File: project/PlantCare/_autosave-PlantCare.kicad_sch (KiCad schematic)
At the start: 34 parts, among them J1 Conn_01x06_Female, J2 USB_C_6pin, J3 Conn_01x02_Female, SW1 SW_DPDT_x2, SW2 SW_Push, SW3 SW_Push, U1 SPX3819M5-L-3-3, U2 ESP-12E, U3 TFT_1.3_12, U4 TP4056_[C16581]

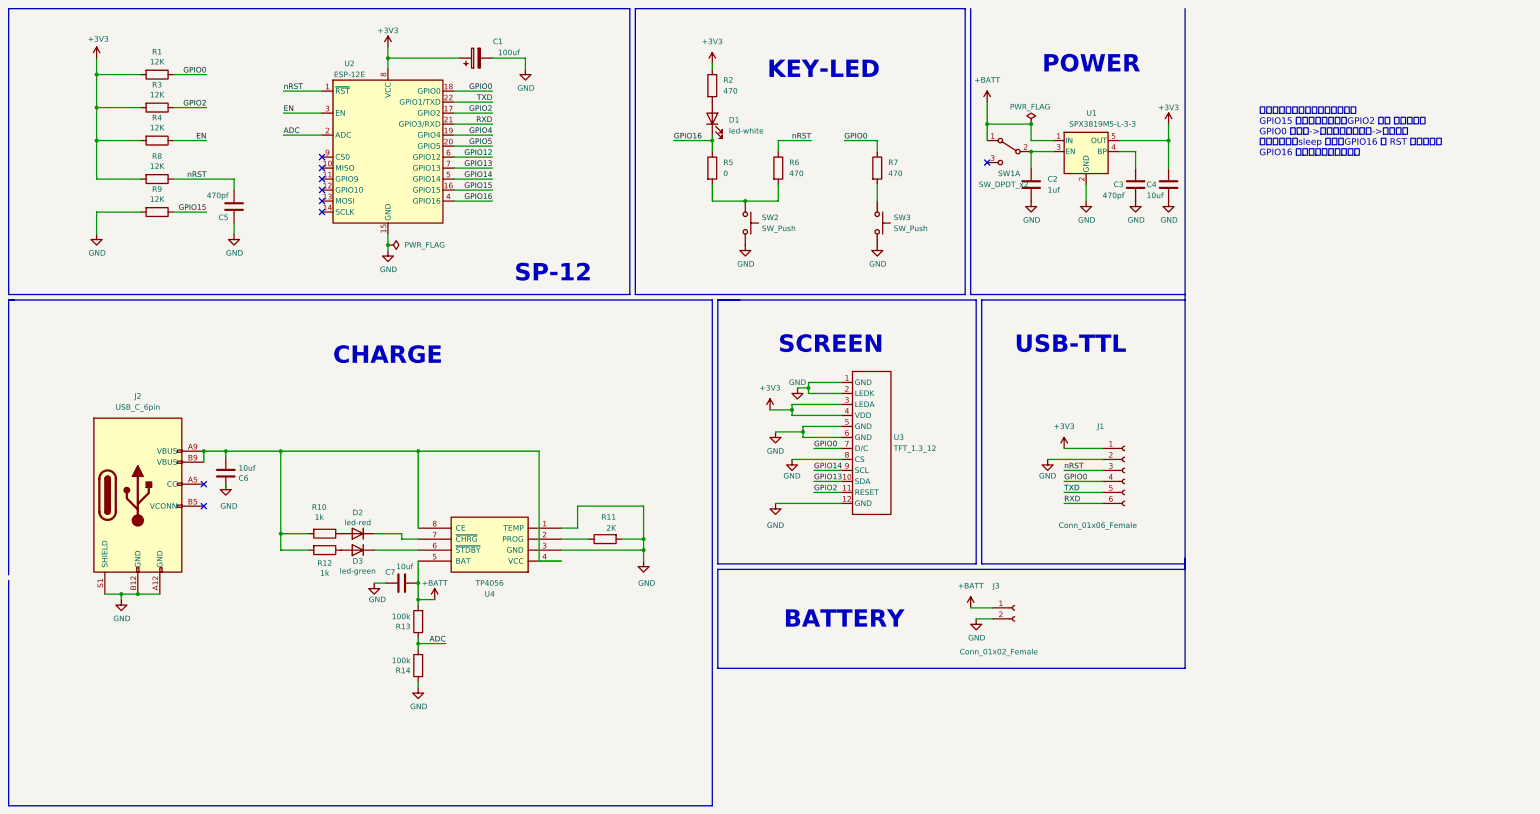
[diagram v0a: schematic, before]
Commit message: fix: screen rst and cs
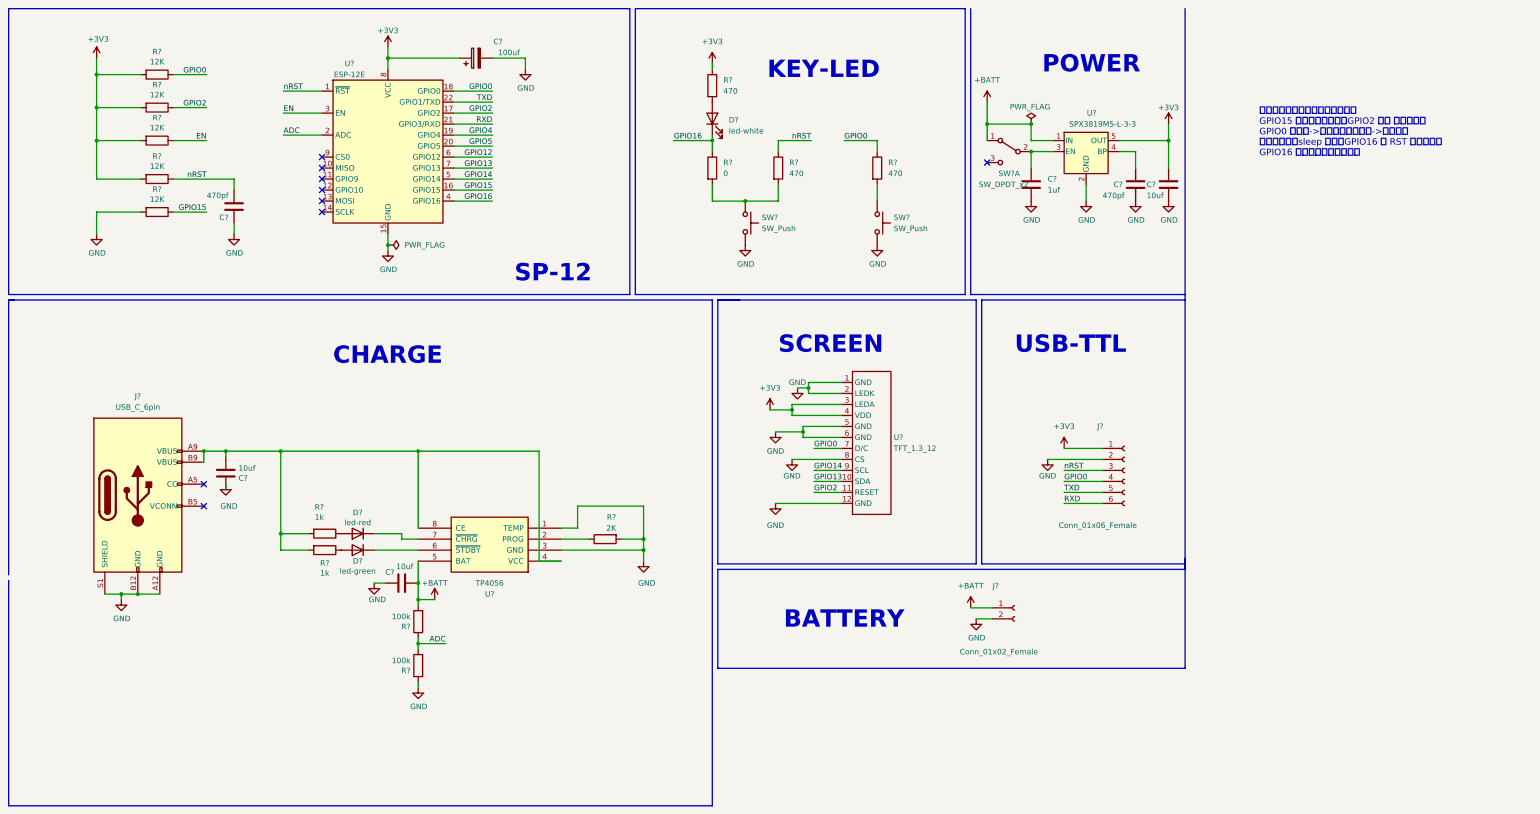
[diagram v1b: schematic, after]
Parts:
- removed C1: 100uf, lc_lib:CASE-B_3528, symbol Device:C_Polarized
- removed C2: 1uf, Capacitor_SMD:C_0402_1005Metric, symbol Device:C
- removed C3, C5: 470pf, Capacitor_SMD:C_0402_1005Metric, symbol Device:C
- removed C4, C6, C7: 10uf, Capacitor_SMD:C_0402_1005Metric, symbol Device:C
- removed D1: led-white, LED_SMD:LED_0402_1005Metric, symbol Device:LED
- removed D2: led-red, LED_SMD:LED_0402_1005Metric, symbol Device:D
- removed D3: led-green, LED_SMD:LED_0402_1005Metric, symbol Device:D
- removed J1: Conn_01x06_Female, Connector_PinHeader_1.27mm:PinHeader_1x06_P1.27mm_Vertical, symbol Connector:Conn_01x06_Female
- removed J2: USB_C_6pin, My-lib-footprints:USB_C_6pin, symbol My-lib:USB_C_6pin
- removed J3: Conn_01x02_Female, Connector_PinHeader_2.54mm:PinHeader_1x02_P2.54mm_Vertical, symbol Connector:Conn_01x02_Female
- removed R1, R3, R4, R8, R9: 12K, Resistor_SMD:R_0402_1005Metric, symbol Device:R
- removed R10, R12: 1k, Resistor_SMD:R_0402_1005Metric, symbol Device:R
- removed R11: 2K, Resistor_SMD:R_0402_1005Metric, symbol Device:R
- removed R13, R14: 100k, Resistor_SMD:R_0402_1005Metric, symbol Device:R
- removed R2, R6, R7: 470, Resistor_SMD:R_0402_1005Metric, symbol Device:R
- removed R5: 0, Resistor_SMD:R_0402_1005Metric, symbol Device:R
- removed SW1: SW_DPDT_x2, Button_Switch_SMD:SW_SPDT_PCM12, symbol Switch:SW_DPDT_x2
- removed SW2, SW3: SW_Push, My-lib:Button_SMD,3x4x2mm, symbol Switch:SW_Push
- removed U1: SPX3819M5-L-3-3, Package_TO_SOT_SMD:SOT-23-5, symbol Regulator_Linear:SPX3819M5-L-3-3
- removed U2: ESP-12E, RF_Module:ESP-12E, symbol RF_Module:ESP-12E
- removed U3: TFT_1.3_12, My-lib-footprints:TFT_1.3_12_front, symbol My-lib:TFT_1.3_12
- removed U4: TP4056_[C16581], lc_lib:SOP-8_EP_150MIL, symbol lc_IC:TP4056_[C16581]
- added C?: 100uf, lc_lib:CASE-B_3528, symbol Device:C_Polarized
- added C? (x3): 10uf, Capacitor_SMD:C_0402_1005Metric, symbol Device:C
- added C? (x2): 470pf, Capacitor_SMD:C_0402_1005Metric, symbol Device:C
- added C?: 1uf, Capacitor_SMD:C_0402_1005Metric, symbol Device:C
- added D?: led-red, LED_SMD:LED_0402_1005Metric, symbol Device:D
- added D?: led-white, LED_SMD:LED_0402_1005Metric, symbol Device:LED
- added D?: led-green, LED_SMD:LED_0402_1005Metric, symbol Device:D
- added J?: Conn_01x02_Female, Connector_PinHeader_2.54mm:PinHeader_1x02_P2.54mm_Vertical, symbol Connector:Conn_01x02_Female
- added J?: USB_C_6pin, My-lib-footprints:USB_C_6pin, symbol My-lib:USB_C_6pin
- added J?: Conn_01x06_Female, Connector_PinHeader_1.27mm:PinHeader_1x06_P1.27mm_Vertical, symbol Connector:Conn_01x06_Female
- added R? (x3): 470, Resistor_SMD:R_0402_1005Metric, symbol Device:R
- added R? (x5): 12K, Resistor_SMD:R_0402_1005Metric, symbol Device:R
- added R?: 2K, Resistor_SMD:R_0402_1005Metric, symbol Device:R
- added R? (x2): 1k, Resistor_SMD:R_0402_1005Metric, symbol Device:R
- added R?: 0, Resistor_SMD:R_0402_1005Metric, symbol Device:R
- added R? (x2): 100k, Resistor_SMD:R_0402_1005Metric, symbol Device:R
- added SW? (x2): SW_Push, My-lib:Button_SMD,3x4x2mm, symbol Switch:SW_Push
- added SW?: SW_DPDT_x2, Button_Switch_SMD:SW_SPDT_PCM12, symbol Switch:SW_DPDT_x2
- added U?: ESP-12E, RF_Module:ESP-12E, symbol RF_Module:ESP-12E
- added U?: TFT_1.3_12, My-lib-footprints:TFT_1.3_12_front, symbol My-lib:TFT_1.3_12
- added U?: TP4056_[C16581], lc_lib:SOP-8_EP_150MIL, symbol lc_IC:TP4056_[C16581]
- added U?: SPX3819M5-L-3-3, Package_TO_SOT_SMD:SOT-23-5, symbol Regulator_Linear:SPX3819M5-L-3-3
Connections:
- net +3V3: now also C?.1, C?.1, J?.1 (Pin_1), R?.1, R?.2, R?.2, R?.2, R?.2, U?.3 (LEDA), U?.4 (VDD), U?.5 (OUT), U?.8 (VCC)
- net +BATT: now also C?.1, J?.1 (Pin_1), R?.2, SW?.1 (A), U?.1 (IN), U?.5 (BAT)
- net ADC: now also R?.1, R?.2, U?.2 (ADC)
- net EN: now also R?.1, U?.3 (EN)
- net GND: now also C?.1, C?.1, C?.2, C?.2, C?.2, C?.2, C?.2, J?.2 (Pin_2), J?.2 (Pin_2), J?.A12 (GND), J?.B12 (GND), J?.S1 (SHIELD), R?.1, R?.2, R?.2, SW?.2, SW?.2, U?.1 (GND), U?.1 (TEMP), U?.12 (GND), U?.15 (GND), U?.2 (GND), U?.2 (LEDK), U?.3 (GND), U?.5 (GND), U?.6 (GND), U?.8 (CS)
- net GPIO0: now also J?.4 (Pin_4), R?.1, R?.1, U?.18 (GPIO0), U?.7 (D/C)
- net GPIO12: now also U?.6 (GPIO12)
- net GPIO13: now also U?.10 (SDA), U?.7 (GPIO13)
- net GPIO14: now also U?.5 (GPIO14), U?.9 (SCL)
- net GPIO15: now also R?.1, U?.16 (GPIO15)
- net GPIO16: now also D?.1 (K), R?.1, U?.4 (GPIO16)
- net GPIO2: now also R?.1, U?.11 (RESET), U?.17 (GPIO2)
- net GPIO4: now also U?.19 (GPIO4)
- net GPIO5: now also U?.20 (GPIO5)
- net RXD: now also J?.6 (Pin_6), U?.21 (GPIO3/RXD)
- net TXD: now also J?.5 (Pin_5), U?.22 (GPIO1/TXD)
- net nRST: now also C?.2, J?.3 (Pin_3), R?.1, R?.1, U?.1 (~{RST})
- new net: R?.2, SW?.1
- new net: D?.2 (A), R?.2
- new net: R?.1, U?.2 (PROG)
- new net: C?.2, J?.A9 (VBUS), J?.B9 (VBUS), R?.2, R?.2, U?.4 (VCC), U?.8 (CE)
- new net: D?.1 (K), U?.7 (~{CHRG})
- new net: D?.2 (A), R?.1 (x2)
- new net: D?.1 (K), U?.6 (~{STDBY})
- new net: R?.2, R?.2, SW?.1
- new net: C?.1, SW?.2 (B), U?.3 (EN)
- new net: C?.1, U?.4 (BP)
